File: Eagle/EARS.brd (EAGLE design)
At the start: 30.7 x 44.5 mm, 23 parts, among them J1 1X2-3.5MM, J2 CORTEX_DEBUG_SMD, X1 ECX_34G

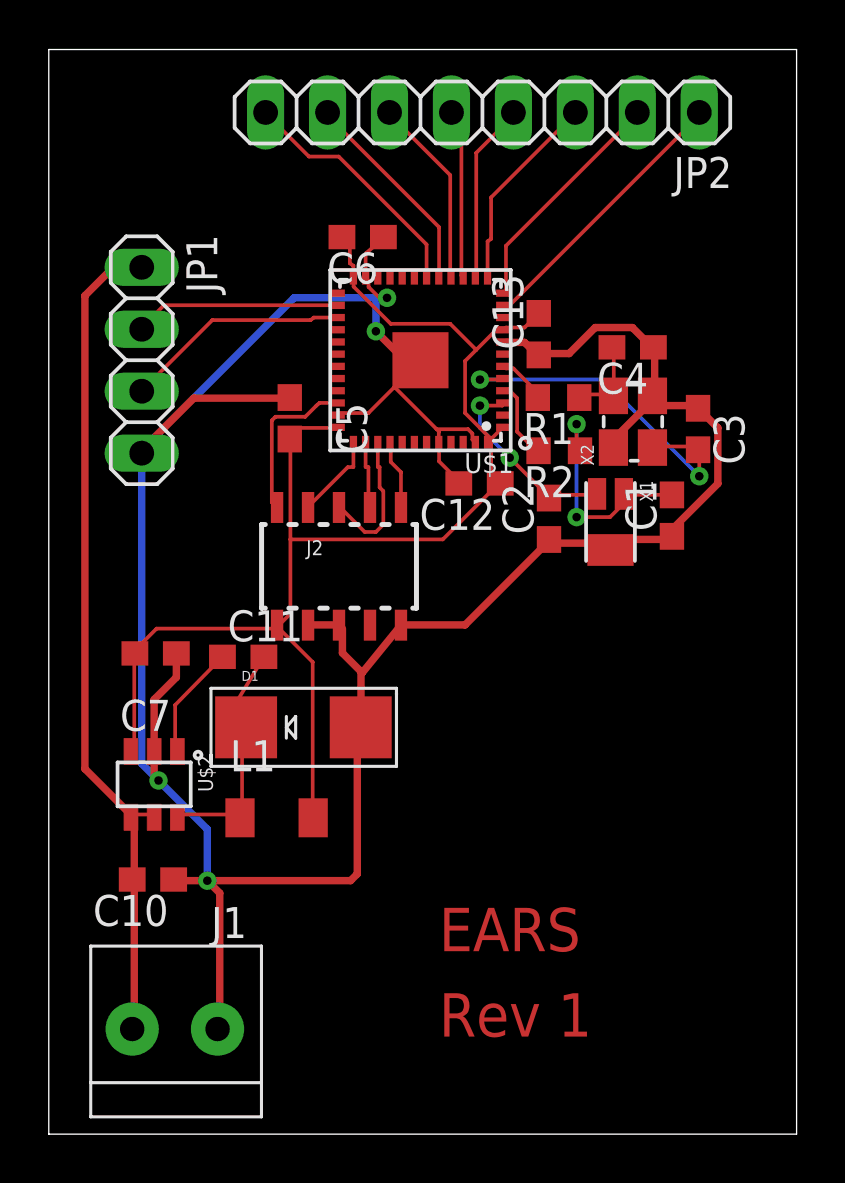
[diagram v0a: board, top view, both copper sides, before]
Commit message: Fixed schematics, added sense circuitry, added solenoid switch circuitry.  Finished layout Rev 1.1
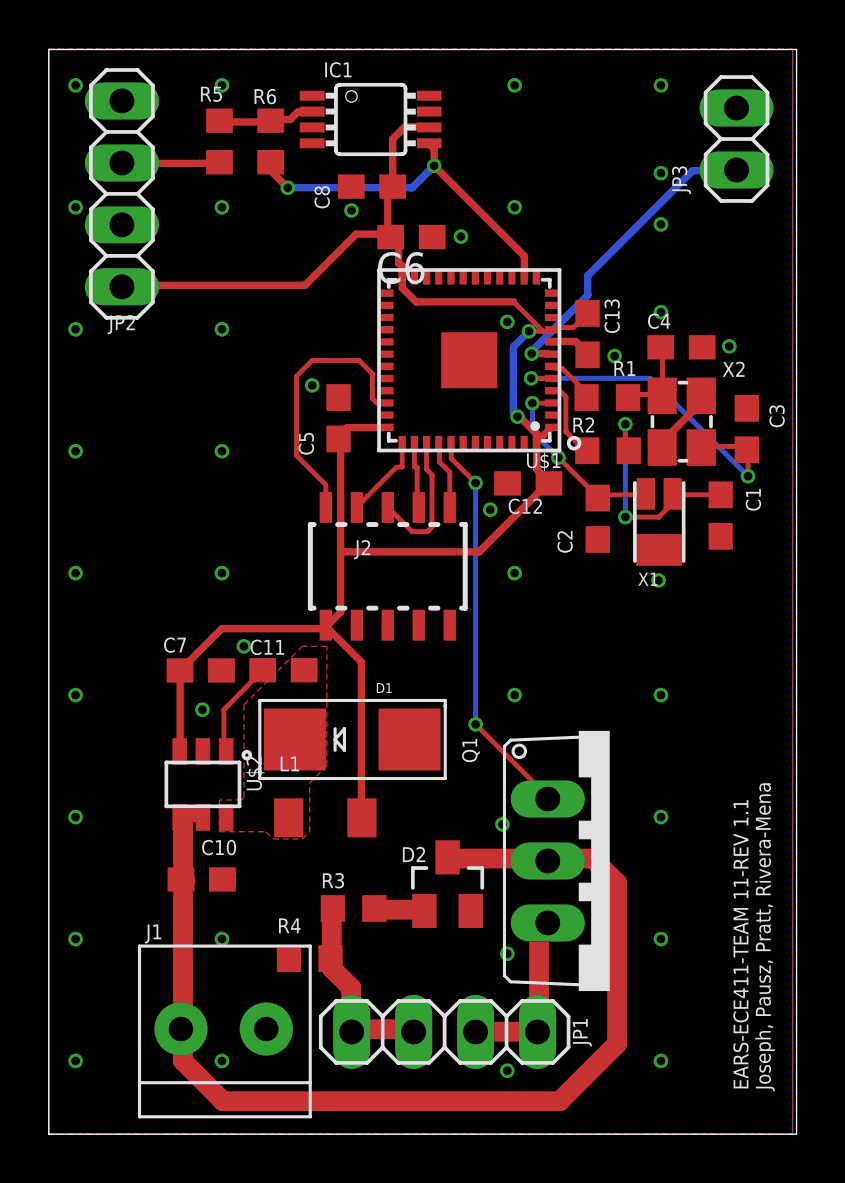
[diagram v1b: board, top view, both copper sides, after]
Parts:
- added C8: 10u, rcl:C0603
- added D2: BAS40, diode:SOT23
- added IC1: LM386MM-1, linear:MMSOP08
- added JP3: (no value), pinhead:1X02
- added Q1: IRLb8721, adafruit:TO220V
- added R3: 28k, rcl:R0603
- added R4: 0, rcl:R0603
- added R5: 1k, rcl:R0603
- added R6: 10k, rcl:R0603
- JP2: device pinhead:1X08 -> pinhead:1X04
- moved JP1 30.2 mm to (16.2, 4.19), turned to 180 degrees
- moved JP2 15.2 mm to (3.00, 38.5), turned to 90 degrees
- moved D1 2.06 mm to (12.4, 16.2)
- moved C1 2.00 mm to (27.6, 25.4)
- moved C10 2.00 mm to (6.27, 10.4)
- moved C12 2.00 mm to (19.7, 26.7)
- moved C13 2.00 mm to (22.1, 32.8)
- moved C2 2.00 mm to (22.5, 25.2)
- moved C3 2.00 mm to (28.6, 28.9)
- moved C4 2.00 mm to (25.9, 32.3)
- moved C5 2.00 mm to (11.9, 29.4)
- moved C6 2.00 mm to (14.9, 36.8)
- moved J1 2.00 mm to (7.12, 4.31)
- moved J2 2.00 mm to (13.9, 23.3)
- moved L1 2.00 mm to (11.3, 13.0)
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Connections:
- removed net P_IN1: JP2.5, U$1.15
- removed net P_IN2: JP2.6, U$1.16
- removed net P_IN3: JP2.7, U$1.17
- removed net P_IN4: JP2.8, U$1.18
- removed net P_OUT1: JP2.1, U$1.11
- removed net P_OUT2: JP2.2, U$1.12
- removed net P_OUT3: JP2.3, U$1.13
- removed net P_OUT4: JP2.4, U$1.14
- removed net SOL_1: JP1.2, U$1.26
- removed net SOL_2: JP1.3, U$1.27
- new net AGND: JP1.3, JP1.4, R3.1, R4.1
- new net FB: IC1.2, R5.2, R6.1
- new net FLYBACK: D2.1, R3.2
- new net NPN: JP1.1, JP1.2, Q1.3
- new net NPN_DRV: Q1.1, U$1.41
- new net NRST: JP3.2, U$1.7
- new net PRESSURE: IC1.5, R6.2, U$1.14
- new net PRSR_IN: JP2.3, R5.1
- net 12V: now also D2.3, Q1.2; no longer JP1.1
- net 3V3: now also C8.2, IC1.6, JP2.1
- net GND: now also C8.1, IC1.3, IC1.4, JP2.2, JP2.4, JP3.1, R4.2; no longer JP1.4
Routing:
- net GND: track 126.8 -> 4.29 mm, vias 4 -> 41
- net 3V3: track 57.4 -> 75.4 mm, vias 0 -> 2
- net NPN_DRV: track 0.00 -> 16.3 mm, vias 0 -> 2
- net PRESSURE: track 0.00 -> 14.9 mm, vias 0 -> 2
- net NRST: track 0.00 -> 12.7 mm, vias 0 -> 1
- net P_OUT1: track 11.4 -> 0.00 mm
- net P_IN4: track 10.2 -> 0.00 mm
- net P_OUT2: track 9.69 -> 0.00 mm
- net 12V: track 34.9 -> 44.6 mm
- net SOL_2: track 9.31 -> 0.00 mm
- net P_IN3: track 8.68 -> 0.00 mm
- net SOL_1: track 8.50 -> 0.00 mm
- net P_OUT3: track 8.29 -> 0.00 mm
- net AGND: track 0.00 -> 7.86 mm
- net LMR_SW: track 10.0 -> 2.18 mm
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- added copper zone on layer 1, net GND
- added copper zone on layer 16, net GND
- added copper zone on layer 1, net LMR_SW
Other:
- board text added: "EARS-ECE411-TEAM 11-REV 1.1 Joseph, Pausz, Pratt, Rivera-Mena"
- board text removed: "EARS"
- board text removed: "Rev 1"
